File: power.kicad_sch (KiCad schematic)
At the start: 34 parts, among them J20 Conn_01x02_Pin, J21 Conn_01x02_Pin, J8 UJC-HP-L-G-5-MSMT-TR, U2 TPS2117DRLR, U3 INA260AIPW, U4 AZ1117IH-3.3TRG1

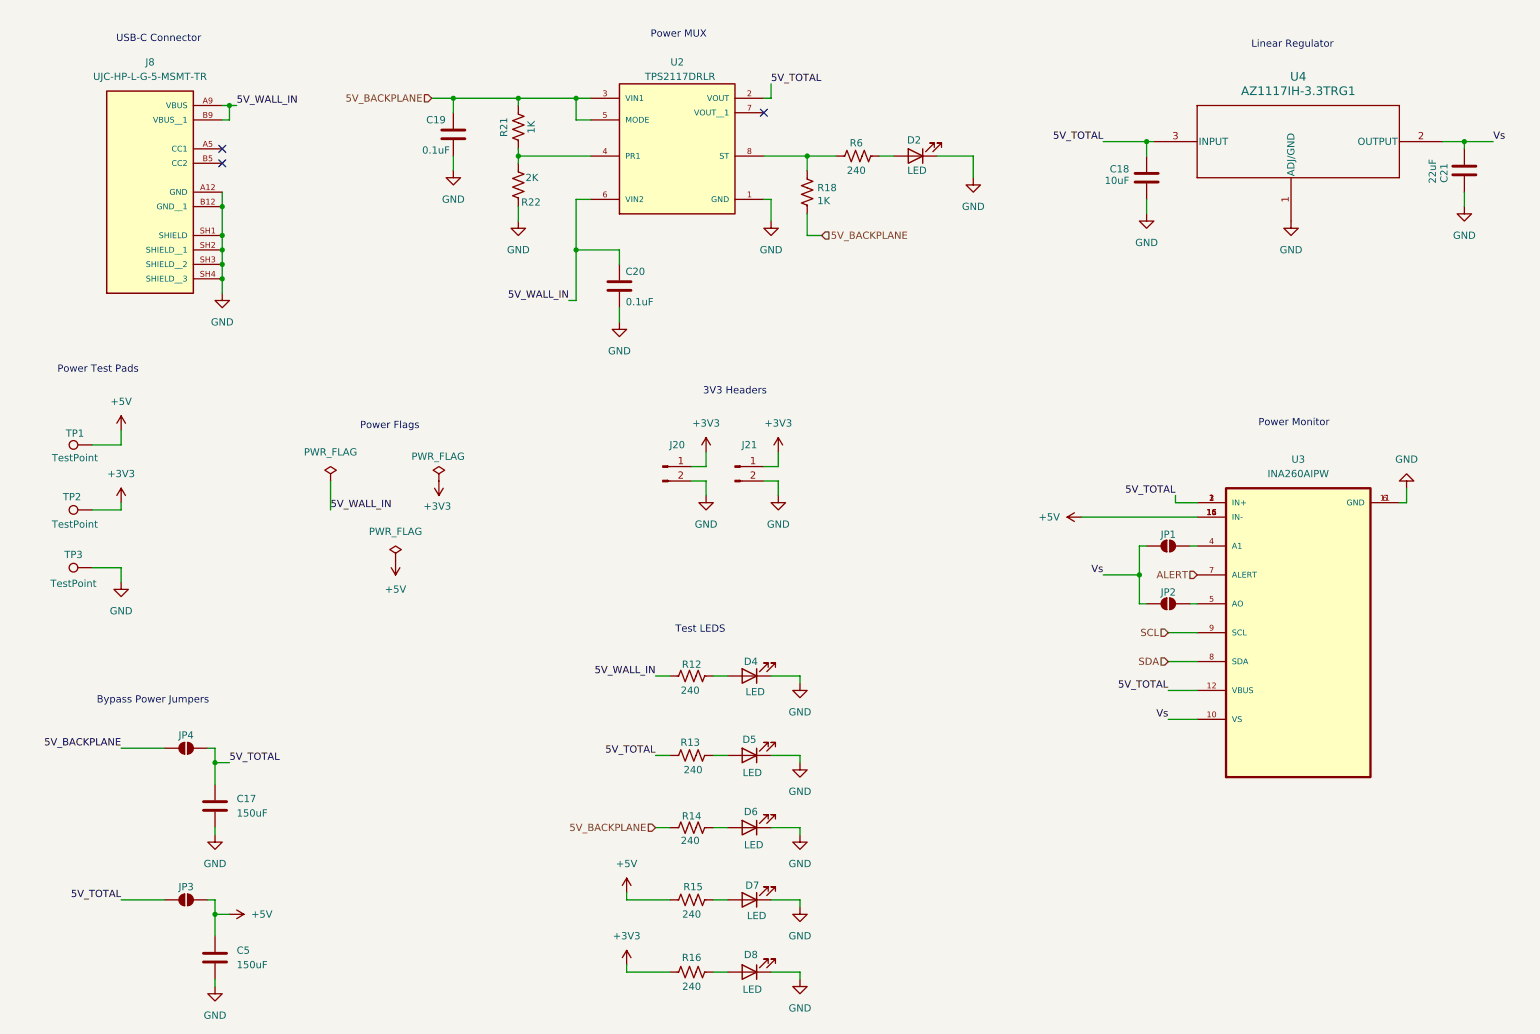
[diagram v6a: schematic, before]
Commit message: Sensor Connector Update
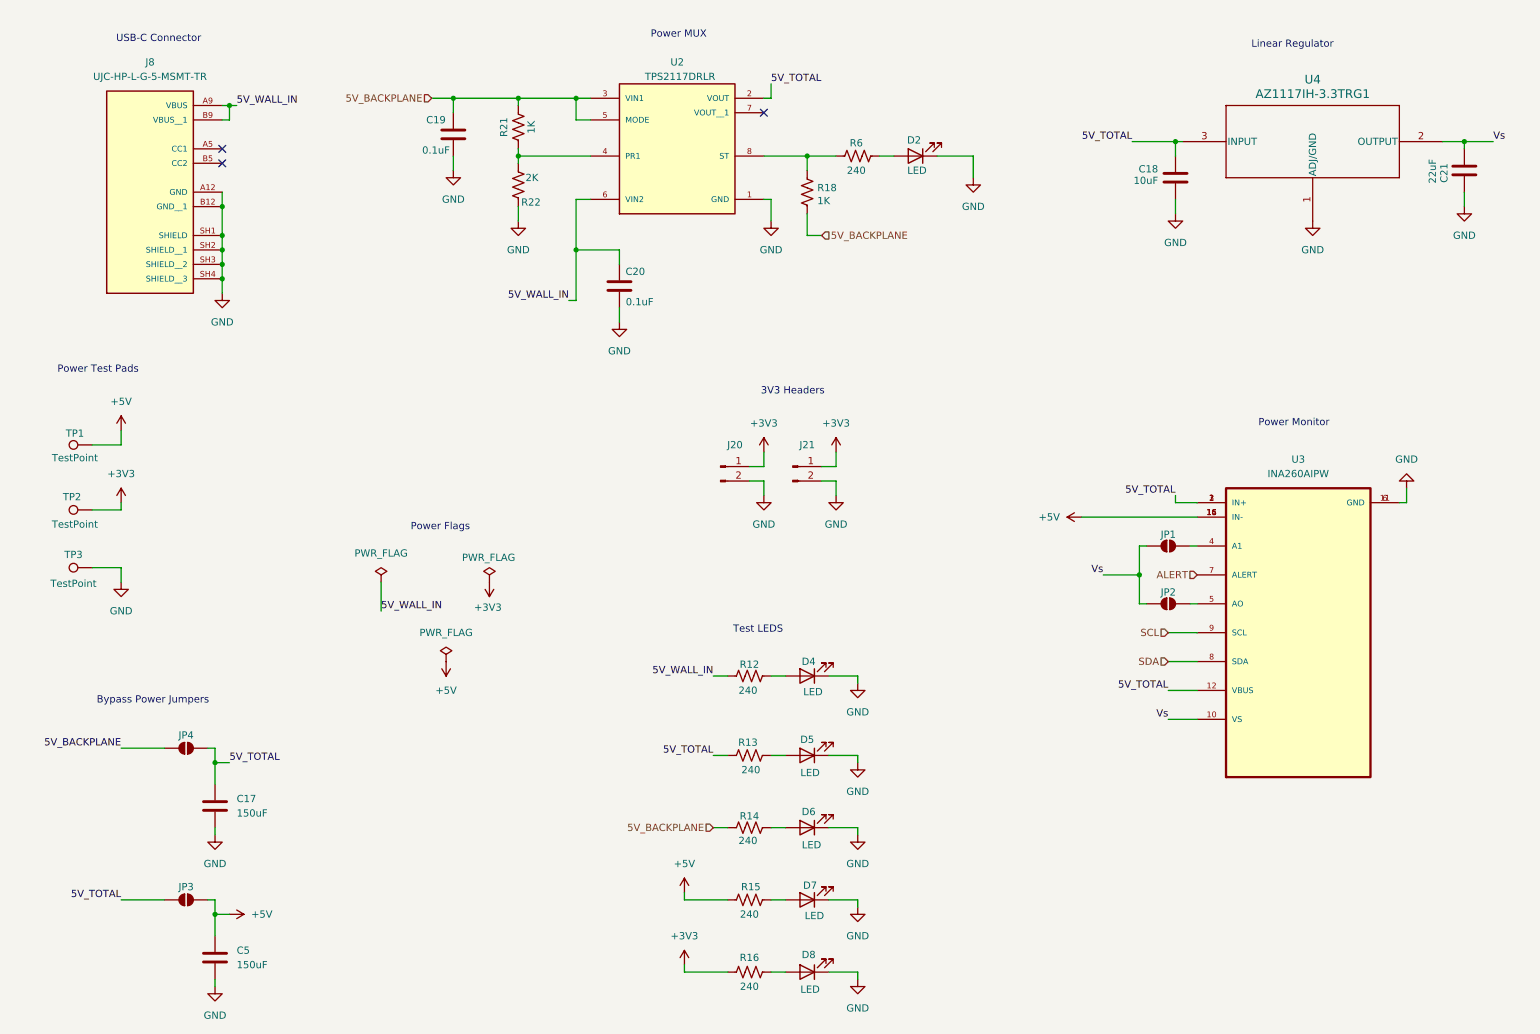
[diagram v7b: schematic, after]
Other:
- moved on the sheet: C18, D4, D5, D6, D7, D8, J20, J21, R12, R13, R14, R15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

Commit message: Pre-Toolbox Final
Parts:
- C17, C18, C19, C20, C21, C5: footprint (none) -> Capacitor_SMD:C_0805_2012Metric_Pad1.18x1.45mm_HandSolder
- D2, D4, D5, D6, D7, D8: footprint (none) -> LED_SMD:LED_0805_2012Metric_Pad1.15x1.40mm_HandSolder
- J20, J21: footprint (none) -> Connector_PinHeader_2.54mm:PinHeader_1x02_P2.54mm_Vertical
- J8: footprint UJC-HP-L-G-5-MSMT-TR:CUI_UJC-HP-L-G-5-MSMT-TR -> UJC_HP_L_G_5_MSMT_TR:CUI_UJC-HP-L-G-5-MSMT-TR
- JP1, JP2, JP3, JP4: footprint (none) -> Jumper:SolderJumper-2_P1.3mm_Open_RoundedPad1.0x1.5mm
- R12, R13, R14, R15, R16, R18, R21, R22, R6: footprint (none) -> Resistor_SMD:R_0805_2012Metric_Pad1.20x1.40mm_HandSolder
- U4: footprint SOT223_AZ1117I_6P5X3P5_DIO -> (none)
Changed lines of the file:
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@@
 			)
 		)
-		(property "Footprint" ""
+		(property "Footprint" "Capacitor_SMD:C_0805_2012Metric_Pad1.18x1.45mm_HandSolder"
 			(at 121.6152 69.85 0)
 			(effects
@@
 			)
 		)
-		(property "Footprint" ""
+		(property "Footprint" "Jumper:SolderJumper-2_P1.3mm_Open_RoundedPad1.0x1.5mm"
 			(at 44.45 173.99 0)
 			(effects
@@
 			)
 		)
-		(property "Footprint" ""
+		(property "Footprint" "Jumper:SolderJumper-2_P1.3mm_Open_RoundedPad1.0x1.5mm"
 			(at 44.45 147.32 0)
 			(effects
@@
 			)
 		)
-		(property "Footprint" ""
+		(property "Footprint" "Jumper:SolderJumper-2_P1.3mm_Open_RoundedPad1.0x1.5mm"
 			(at 217.17 121.92 0)
 			(effects
@@
 			)
 		)
-		(property "Footprint" ""
+		(property "Footprint" "LED_SMD:LED_0805_2012Metric_Pad1.15x1.40mm_HandSolder"
 			(at 172.72 43.18 0)
 			(effects
@@
 			)
 		)
-		(property "Footprint" ""
+		(property "Footprint" "Capacitor_SMD:C_0805_2012Metric_Pad1.18x1.45mm_HandSolder"
 			(at 50.4952 161.29 0)
 			(effects
@@
 			)
 		)
-		(property "Footprint" ""
+		(property "Footprint" "Jumper:SolderJumper-2_P1.3mm_Open_RoundedPad1.0x1.5mm"
 			(at 217.17 111.76 0)
 			(effects
@@
 			)
 		)
-		(property "Footprint" ""
+		(property "Footprint" "Resistor_SMD:R_0805_2012Metric_Pad1.20x1.40mm_HandSolder"
 			(at 143.764 160.274 90)
 			(effects
@@
 			)
 		)
-		(property "Footprint" "UJC-HP-L-G-5-MSMT-TR:CUI_UJC-HP-L-G-5-MSMT-TR"
+		(property "Footprint" "UJC_HP_L_G_5_MSMT_TR:CUI_UJC-HP-L-G-5-MSMT-TR"
 			(at 38.1 41.91 0)
 			(effects
@@
 			)
 		)
-		(property "Footprint" ""
+		(property "Footprint" "LED_SMD:LED_0805_2012Metric_Pad1.15x1.40mm_HandSolder"
 			(at 153.67 173.99 0)
 			(effects
@@
 			)
 		)
-		(property "Footprint" ""
+		(property "Footprint" "Resistor_SMD:R_0805_2012Metric_Pad1.20x1.40mm_HandSolder"
 			(at 143.764 133.604 90)
 			(effects
@@
 			)
 		)
-		(property "Footprint" ""
+		(property "Footprint" "Resistor_SMD:R_0805_2012Metric_Pad1.20x1.40mm_HandSolder"
 			(at 103.886 48.514 90)
 			(effects
@@
 			)
 		)
-		(property "Footprint" ""
+		(property "Footprint" "Connector_PinHeader_2.54mm:PinHeader_1x02_P2.54mm_Vertical"
 			(at 151.13 97.79 0)
 			(effects
@@
 			)
 		)
-		(property "Footprint" ""
+		(property "Footprint" "Resistor_SMD:R_0805_2012Metric_Pad1.20x1.40mm_HandSolder"
 			(at 103.886 38.354 90)
 			(effects
@@
 			)
 		)
-		(property "Footprint" ""
+		(property "Footprint" "LED_SMD:LED_0805_2012Metric_Pad1.15x1.40mm_HandSolder"
 			(at 153.67 148.59 0)
 			(effects
@@
 			)
 		)
-		(property "Footprint" ""
+		(property "Footprint" "Resistor_SMD:R_0805_2012Metric_Pad1.20x1.40mm_HandSolder"
 			(at 162.814 42.164 90)
 			(effects
@@
 			)
 		)
-		(property "Footprint" ""
+		(property "Footprint" "Resistor_SMD:R_0805_2012Metric_Pad1.20x1.40mm_HandSolder"
 			(at 154.686 49.784 90)
 			(effects
@@
 			)
 		)
-		(property "Footprint" ""
+		(property "Footprint" "Capacitor_SMD:C_0805_2012Metric_Pad1.18x1.45mm_HandSolder"
 			(at 50.4952 187.96 0)
 			(effects
@@
 			)
 		)
-		(property "Footprint" ""
+		(property "Footprint" "Resistor_SMD:R_0805_2012Metric_Pad1.20x1.40mm_HandSolder"
 			(at 143.764 185.674 90)
 			(effects
@@
 			)
 		)
-		(property "Footprint" ""
+		(property "Footprint" "Capacitor_SMD:C_0805_2012Metric_Pad1.18x1.45mm_HandSolder"
 			(at 219.4052 50.8 0)
 			(effects
@@
 			)
 		)
-		(property "Footprint" ""
+		(property "Footprint" "LED_SMD:LED_0805_2012Metric_Pad1.15x1.40mm_HandSolder"
 			(at 153.67 186.69 0)
 			(effects
@@
 			)
 		)
-		(property "Footprint" "SOT223_AZ1117I_6P5X3P5_DIO"
+		(property "Footprint" ""
 			(at 240.538 70.866 0)
 			(effects
@@
 			)
 		)
-		(property "Footprint" ""
+		(property "Footprint" "LED_SMD:LED_0805_2012Metric_Pad1.15x1.40mm_HandSolder"
 			(at 153.67 161.29 0)
 			(effects
@@
 			)
 		)
-		(property "Footprint" ""
+		(property "Footprint" "Capacitor_SMD:C_0805_2012Metric_Pad1.18x1.45mm_HandSolder"
 			(at 90.4748 35.56 0)
 			(effects
@@
 			)
 		)
-		(property "Footprint" ""
+		(property "Footprint" "LED_SMD:LED_0805_2012Metric_Pad1.15x1.40mm_HandSolder"
 			(at 153.67 134.62 0)
 			(effects
@@
 			)
 		)
-		(property "Footprint" ""
+		(property "Footprint" "Capacitor_SMD:C_0805_2012Metric_Pad1.18x1.45mm_HandSolder"
 			(at 270.2052 49.53 0)
 			(effects
@@
 			)
 		)
-		(property "Footprint" ""
+		(property "Footprint" "Connector_PinHeader_2.54mm:PinHeader_1x02_P2.54mm_Vertical"
 			(at 138.43 97.79 0)
 			(effects
@@
 			)
 		)
-		(property "Footprint" ""
+		(property "Footprint" "Resistor_SMD:R_0805_2012Metric_Pad1.20x1.40mm_HandSolder"
 			(at 143.764 172.974 90)
 			(effects
@@
 			)
 		)
-		(property "Footprint" ""
+		(property "Footprint" "Resistor_SMD:R_0805_2012Metric_Pad1.20x1.40mm_HandSolder"
 			(at 143.764 147.574 90)
 			(effects
